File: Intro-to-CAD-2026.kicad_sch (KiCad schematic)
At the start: 6 parts

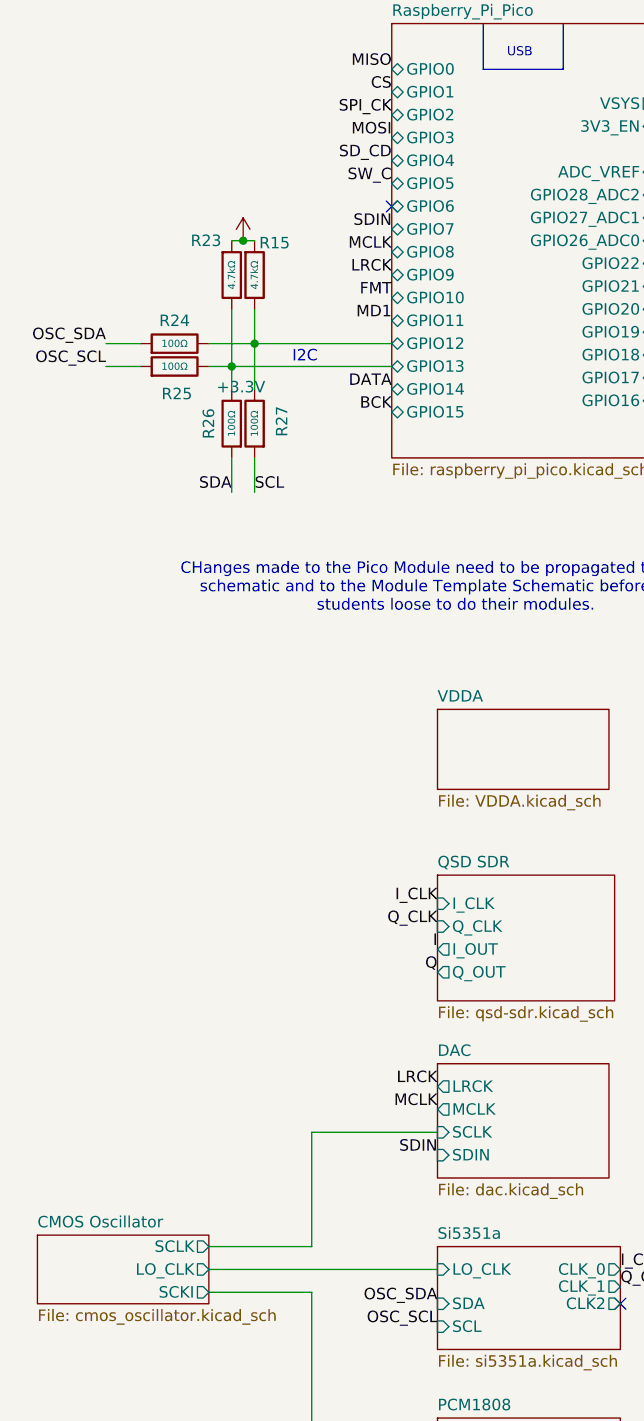
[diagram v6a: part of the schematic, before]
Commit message: Fixed DAC
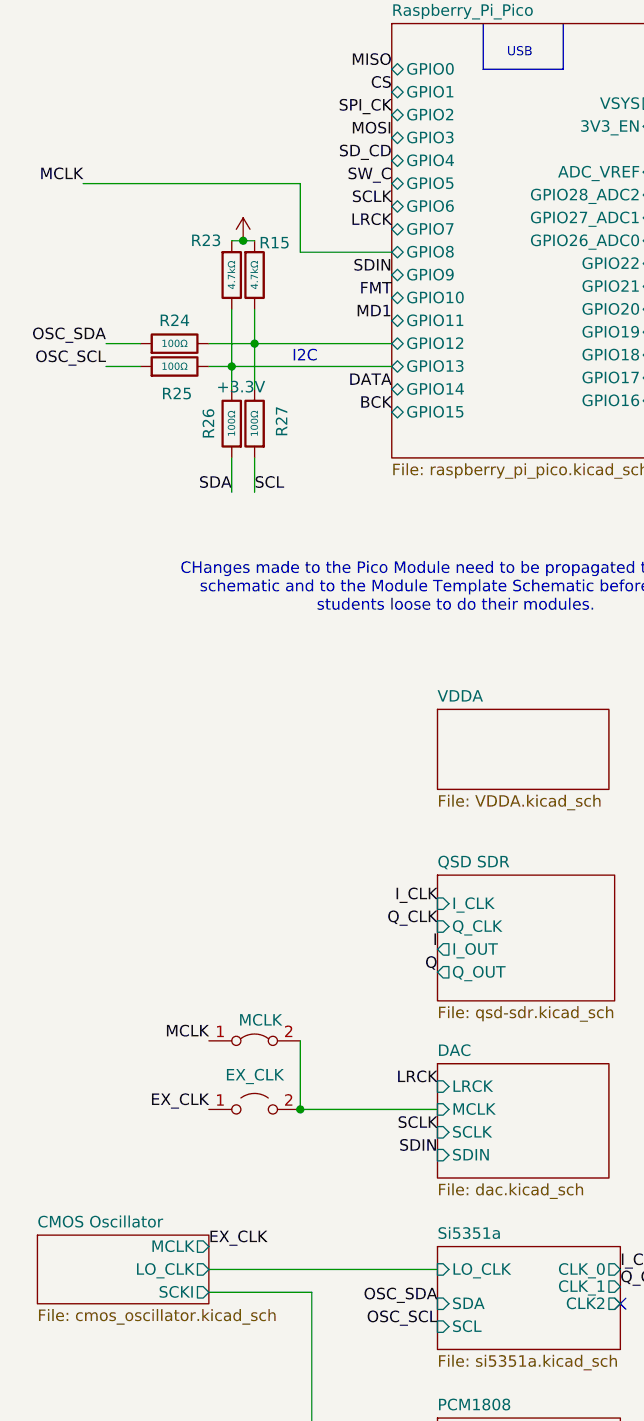
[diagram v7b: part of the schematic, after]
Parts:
- added JP6: EX_CLK, Jumper:SolderJumper-2_P1.3mm_Open_RoundedPad1.0x1.5mm, symbol Jumper:Jumper_2_Open
- added e9: MCLK, Jumper:SolderJumper-2_P1.3mm_Bridged_RoundedPad1.0x1.5mm, symbol Jumper:Jumper_2_Bridged
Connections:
- net MCLK: now also e9.1 (A)
- new net DAC/MCLK: JP6.2 (B), e9.2 (B)
- new net EX_CLK: JP6.1 (A)
- no-connect marks 5 -> 4
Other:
- sheet CMOS Oscillator ports: added MCLK; removed SCLK
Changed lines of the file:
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@@
 	)
 	(junction
+		(at 46.99 140.97)
+		(diameter 0)
+		(color 0 0 0 0)
+	)
+	(junction
 		(at 40.64 44.45)
 		(diameter 0)
@@
 	)
 	(no_connect
-		(at 57.15 40.64)
-	)
-	(no_connect
 		(at 86.36 44.45)
 	)
@@
 	(wire
 		(pts
-			(xy 36.83 58.42) (xy 39.37 58.42)
+			(xy 46.99 38.1) (xy 46.99 45.72)
 		)
 		(stroke
@@
 		)
 	)
-	(polyline
+	(wire
 		(pts
-			(xy 76.2 20.32) (xy 76.2 25.4)
+			(xy 22.86 38.1) (xy 46.99 38.1)
 		)
 		(stroke
@@
 	(wire
 		(pts
-			(xy 91.44 29.21) (xy 86.36 29.21)
+			(xy 36.83 58.42) (xy 39.37 58.42)
 		)
 		(stroke
@@
 	(wire
 		(pts
-			(xy 36.83 156.21) (xy 48.26 156.21)
+			(xy 46.99 133.35) (xy 46.99 140.97)
 		)
 		(stroke
@@
 	(polyline
 		(pts
-			(xy 67.31 20.32) (xy 67.31 25.4)
+			(xy 76.2 20.32) (xy 76.2 25.4)
 		)
 		(stroke
@@
 	(wire
 		(pts
-			(xy 48.26 143.51) (xy 62.23 143.51)
+			(xy 91.44 29.21) (xy 86.36 29.21)
 		)
 		(stroke
@@
 	(wire
 		(pts
-			(xy 25.4 55.88) (xy 29.21 55.88)
+			(xy 62.23 140.97) (xy 46.99 140.97)
+		)
+		(stroke
+			(width 0)
+			(type default)
+		)
+	)
+	(wire
+		(pts
+			(xy 46.99 45.72) (xy 57.15 45.72)
+		)
+		(stroke
+			(width 0)
+			(type default)
+		)
+	)
+	(polyline
+		(pts
+			(xy 67.31 20.32) (xy 67.31 25.4)
 		)
 		(stroke
@@
 	(wire
 		(pts
-			(xy 48.26 156.21) (xy 48.26 143.51)
+			(xy 25.4 55.88) (xy 29.21 55.88)
 		)
 		(stroke
@@
 	)
 	(label "MCLK"
-		(at 62.23 140.97 180)
+		(at 36.83 133.35 180)
 		(effects
 			(font
@@
 		)
 	)
+	(label "EX_CLK"
+		(at 36.83 156.21 0)
+		(effects
+			(font
+				(size 1.27 1.27)
+			)
+			(justify left bottom)
+		)
+	)
 	(label "INB"
 		(at 189.23 69.85 180)
@@
 		)
 	)
+	(label "EX_CLK"
+		(at 36.83 140.97 180)
+		(effects
+			(font
+				(size 1.27 1.27)
+			)
+			(justify right bottom)
+		)
+	)
 	(label "Q_CLK"
 		(at 62.23 120.65 180)
@@
 		)
 	)
+	(label "SCLK"
+		(at 62.23 143.51 180)
+		(effects
+			(font
+				(size 1.27 1.27)
+			)
+			(justify right bottom)
+		)
+	)
 	(label "MCLK"
-		(at 57.15 45.72 180)
+		(at 22.86 38.1 180)
 		(effects
 			(font
@@
 		)
 	)
+	(label "SCLK"
+		(at 57.15 40.64 180)
+		(effects
+			(font
+				(size 1.27 1.27)
+			)
+			(justify right bottom)
+		)
+	)
 	(label "Q"
 		(at 62.23 125.73 180)
@@
 	)
 	(label "SDIN"
-		(at 57.15 43.18 180)
+		(at 57.15 48.26 180)
 		(effects
 			(font
@@
 	)
 	(label "LRCK"
-		(at 57.15 48.26 180)
+		(at 57.15 43.18 180)
 		(effects
 			(font
@@
 	)
 	(symbol
+		(lib_name "Jumper_2_Bridged_1")
+		(lib_id "Jumper:Jumper_2_Bridged")
+		(at 41.91 133.35 0)
+		(unit 1)
+		(exclude_from_sim no)
+		(in_bom yes)
+		(on_board yes)
+		(dnp no)
+		(property "Reference" "e9"
+			(at 43.1801 134.62 90)
+			(effects
+				(font
+					(size 1.27 1.27)
+				)
+				(justify right)
+				(hide yes)
+			)
+		)
+		(property "Value" "MCLK"
+			(at 44.958 131.064 0)
+			(effects
+				(font
+					(size 1.27 1.27)
+				)
+				(justify right)
+			)
+		)
+		(property "Footprint" "Jumper:SolderJumper-2_P1.3mm_Bridged_RoundedPad1.0x1.5mm"
+			(at 41.91 133.35 0)
+			(effects
+				(font
+					(size 1.27 1.27)
+				)
+				(hide yes)
+			)
+		)
+		(property "Datasheet" "~"
+			(at 41.91 133.35 0)
+			(effects
+				(font
+					(size 1.27 1.27)
+				)
+				(hide yes)
+			)
+		)
+		(property "Description" "Jumper, 2-pole, closed/bridged"
+			(at 41.91 133.35 0)
+			(effects
+				(font
+					(size 1.27 1.27)
+				)
+				(hide yes)
+			)
+		)
+		(pin "1"
+		)
+		(pin "2"
+		)
+		(instances
+			(project "Intro-to-CAD-2026"
+				(path "/c12dc015-e6cb-468c-8de4-269c3106de0e"
+					(reference "e9")
+					(unit 1)
+				)
+			)
+		)
+	)
+	(symbol
 		(lib_id "power:+5V")
 		(at 91.44 29.21 270)
@@
 	)
 	(symbol
+		(lib_id "Jumper:Jumper_2_Open")
+		(at 41.91 140.97 0)
+		(unit 1)
+		(exclude_from_sim no)
+		(in_bom yes)
+		(on_board yes)
+		(dnp no)
+		(fields_autoplaced yes)
+		(property "Reference" "JP6"
+			(at 41.91 134.62 0)
+			(effects
+				(font
+					(size 1.27 1.27)
+				)
+				(hide yes)
+			)
+		)
+		(property "Value" "EX_CLK"
+			(at 41.91 137.16 0)
+			(effects
+				(font
+					(size 1.27 1.27)
+				)
+			)
+		)
+		(property "Footprint" "Jumper:SolderJumper-2_P1.3mm_Open_RoundedPad1.0x1.5mm"
+			(at 41.91 140.97 0)
+			(effects
+				(font
+					(size 1.27 1.27)
+				)
+				(hide yes)
+			)
+		)
+		(property "Datasheet" "~"
+			(at 41.91 140.97 0)
+			(effects
+				(font
+					(size 1.27 1.27)
+				)
+				(hide yes)
+			)
+		)
+		(property "Description" ""
+			(at 41.91 140.97 0)
+			(effects
+				(font
+					(size 1.27 1.27)
+				)
+				(hide yes)
+			)
+		)
+		(property "JLCPCB #" ""
+			(at 41.91 140.97 0)
+			(effects
+				(font
+					(size 1.27 1.27)
+				)
+				(hide yes)
+			)
+		)
+		(pin "1"
+		)
+		(pin "2"
+		)
+		(instances
+			(project "Intro-to-CAD-2026"
+				(path "/c12dc015-e6cb-468c-8de4-269c3106de0e"
+					(reference "JP6")
+					(unit 1)
+				)
+			)
+		)
+	)
+	(symbol
 		(lib_id "PCM_JLCPCB-Resistors:0805,4.7kΩ")
 		(at 41.91 48.26 0)
@@
 			)
 		)
-		(pin "SCLK" output
+		(pin "MCLK" output
 			(at 36.83 156.21 0)
 			(effects
@@
 			)
 		)
-		(pin "LRCK" output
+		(pin "LRCK" input
 			(at 62.23 138.43 180)
 			(effects
@@
 			)
 		)
-		(pin "MCLK" output
+		(pin "MCLK" input
 			(at 62.23 140.97 180)
 			(effects

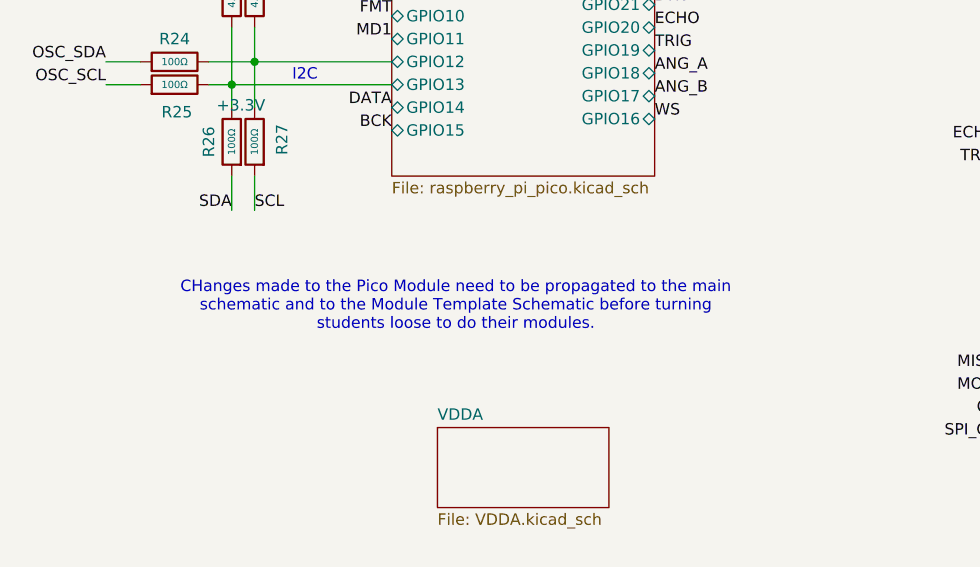
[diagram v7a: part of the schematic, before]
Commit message: Initial v0.2
Fixed SCL-SDA swap, 3V3 on encoder, and 3D models for Kicad 10
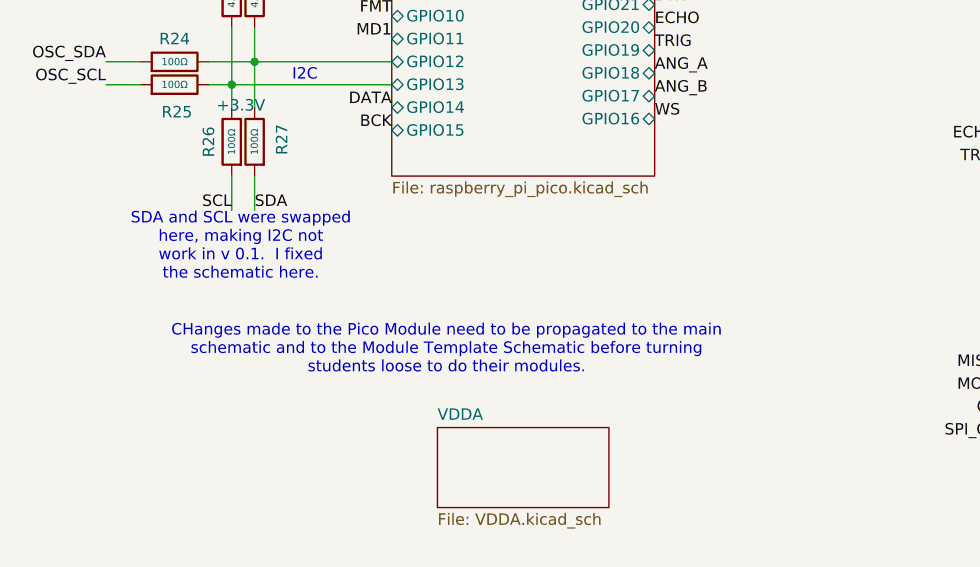
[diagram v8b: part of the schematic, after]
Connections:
- net SCL: now also R26.1; no longer R27.1
- net SDA: now also R27.1; no longer R26.1
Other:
- note added: "SDA and SCL were swapped here, making I2C not work in v 0.1. I fixed the schematic here."
- company: (none) -> Walla Walla University
- title: (none) -> Intro to CAD 2026 Experimenter's Board
